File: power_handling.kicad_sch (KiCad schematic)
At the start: 64 parts, among them J1 usb_c, U1 CUS-12TB, U2 TS3USB221ERSER, U3 TPS62130, U4 AP22802AW5-7, U5 MIC5365-1.8YC5-TR, U6 TPS7A0309PDBVR, U7 TPS62130

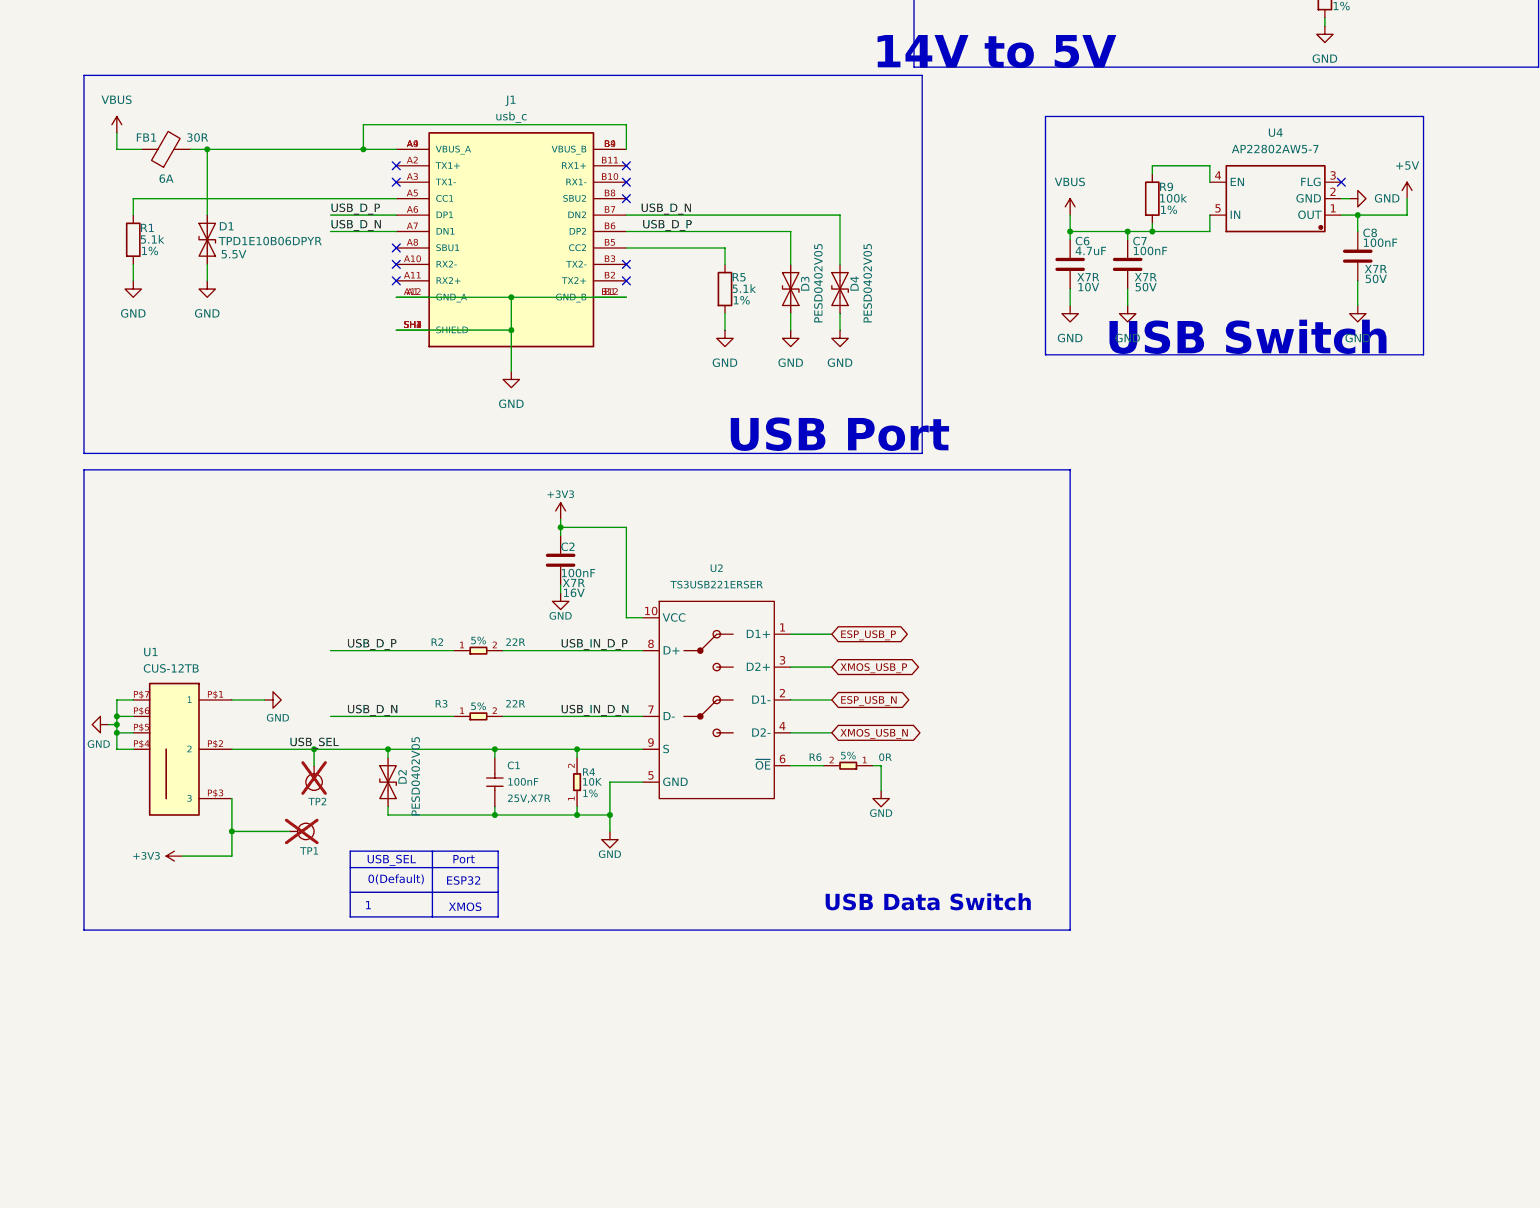
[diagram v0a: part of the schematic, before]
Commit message: adding esp32c6 for OTBR
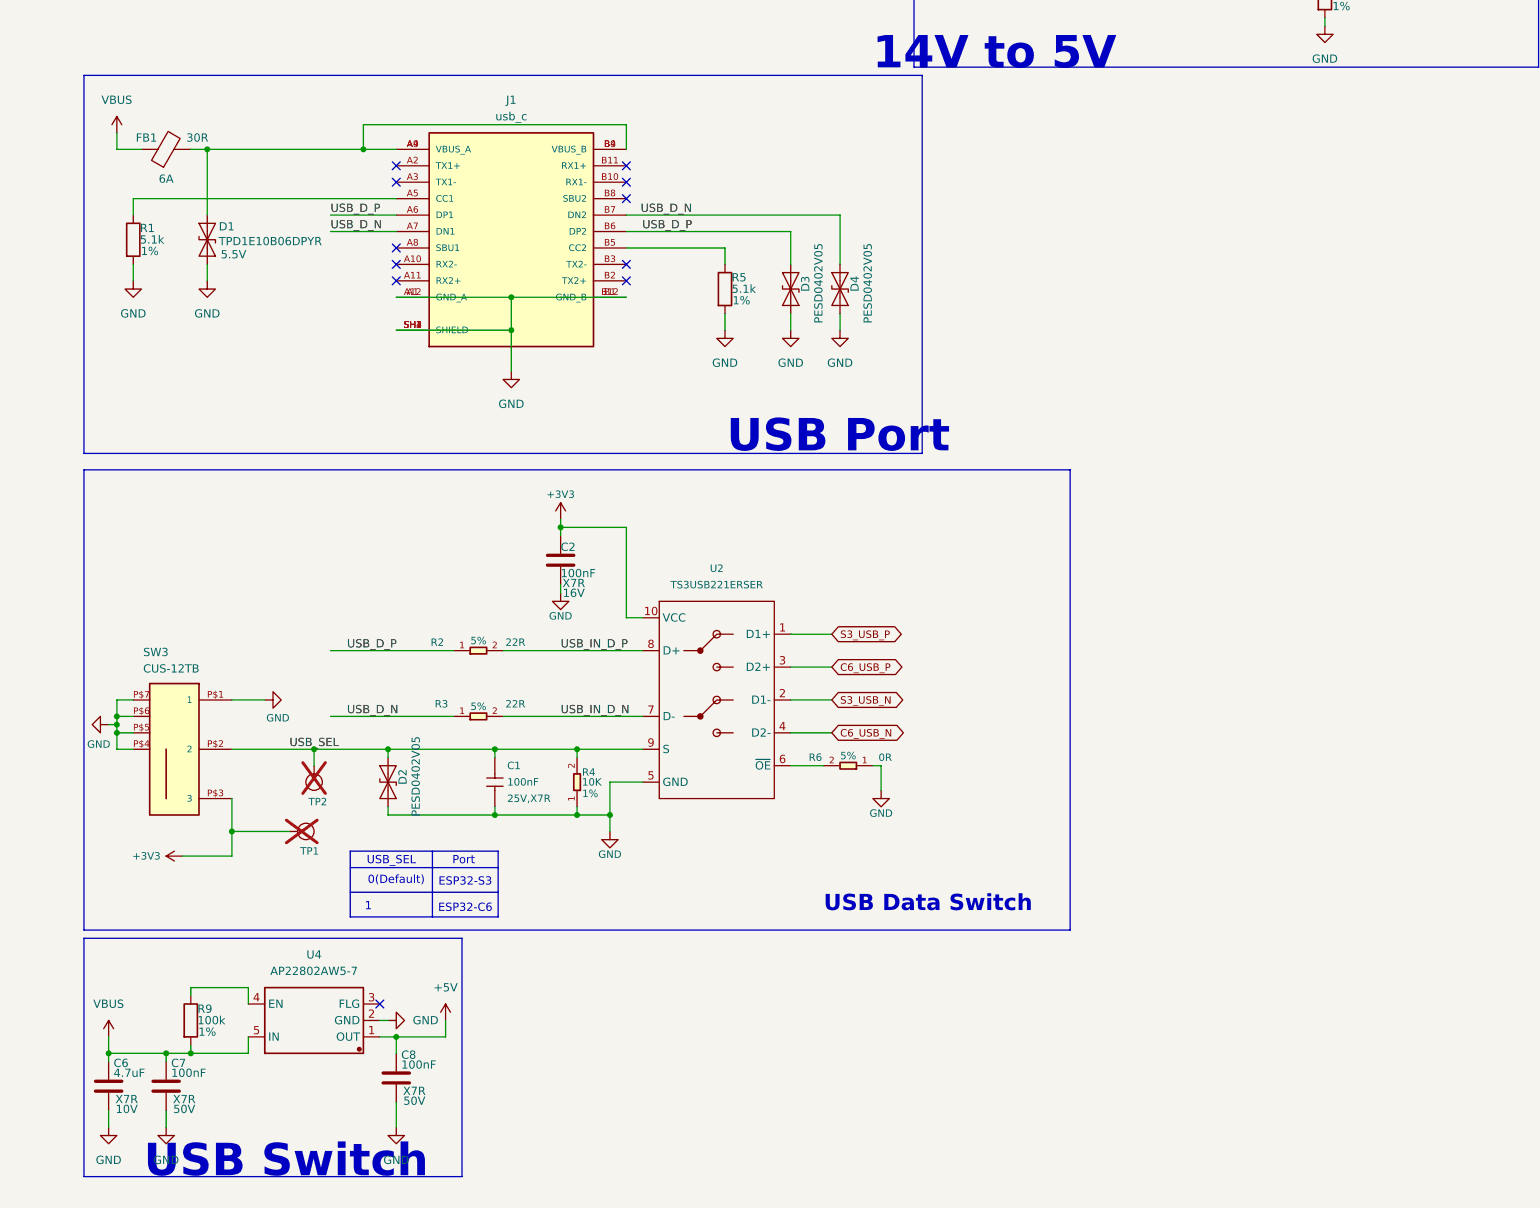
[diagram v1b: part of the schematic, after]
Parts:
- renumbered U1 to SW3
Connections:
- net ESP_USB_N renamed S3_USB_N
- net ESP_USB_P renamed S3_USB_P
- net XMOS_USB_N renamed C6_USB_N
- net XMOS_USB_P renamed C6_USB_P
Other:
- note added: "ESP32-C6"
- note added: "ESP32-S3"
- note removed: "ESP32"
- note removed: "XMOS"
- moved on the sheet: C6, C7, C8, R9, U4

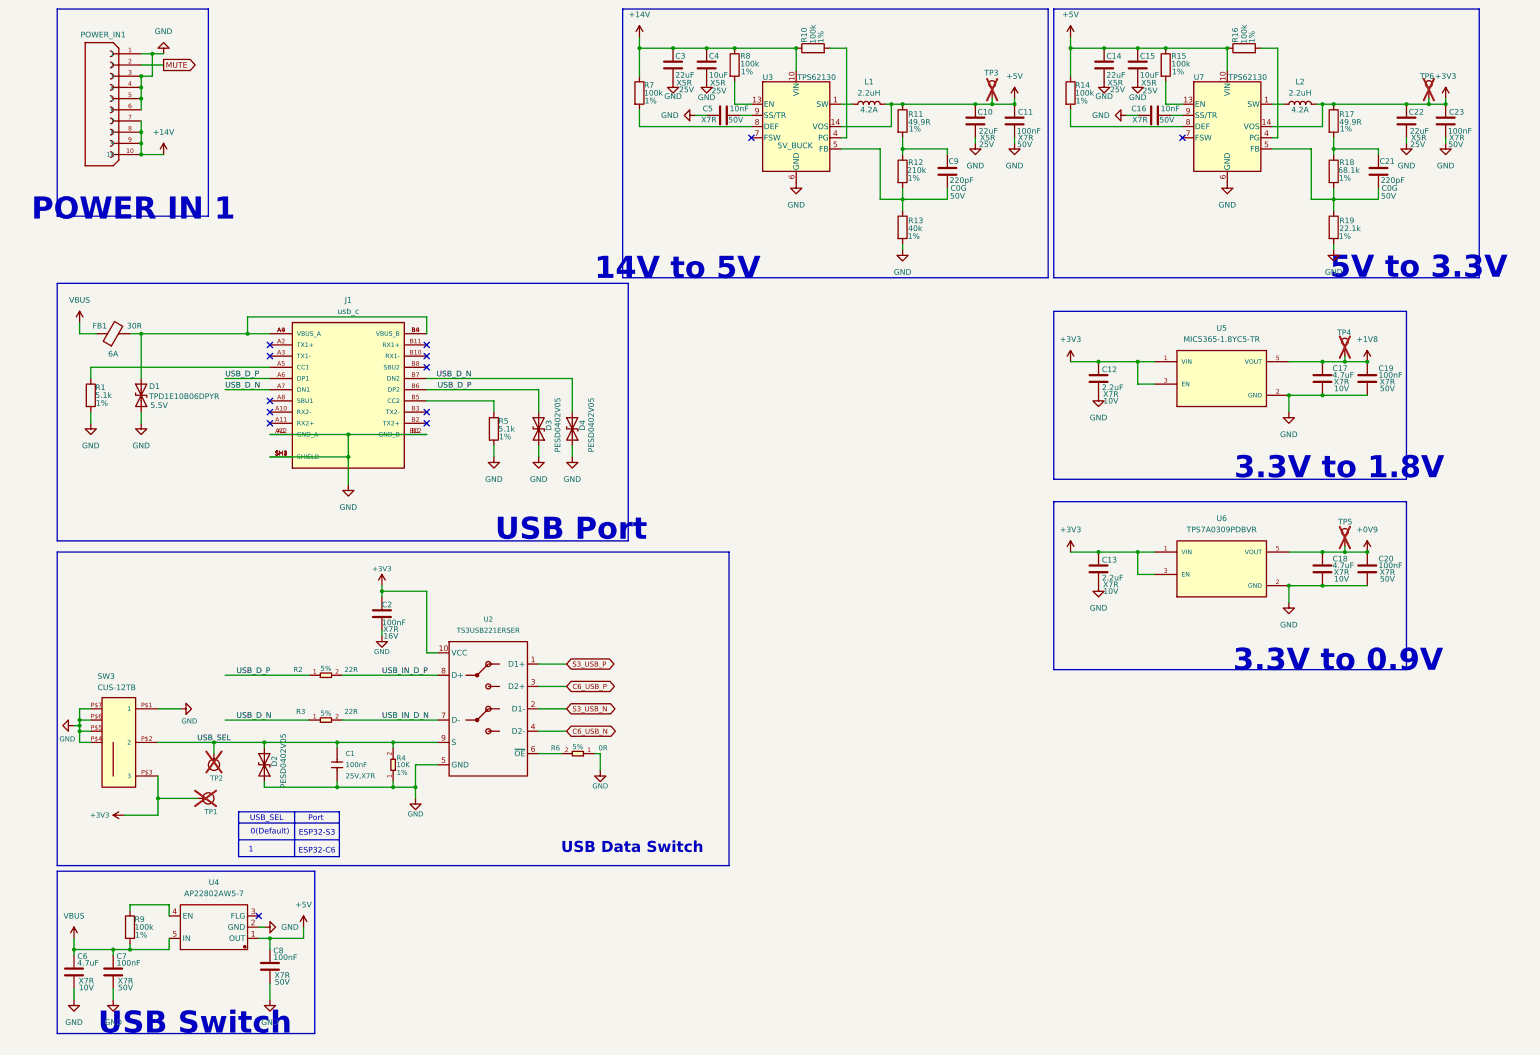
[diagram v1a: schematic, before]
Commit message: Publish KiCad 10 hardware updates
Refresh the Nest Mini v2 drop-in PCB project in KiCad 10 and publish the accumulated schematic and board updates as a single clean mainline change.

Remove the unused USB-C power/input branch from the power sheet, including the USB connector path, data switching, VBUS switching, and associated support parts, while preserving the pogo-accessible USB signals where needed. Add the ESP32-C6 1x05 pogo connector with the J2-style pin order for GND, boot, reset, USB D-, and USB D+ without a 3.3 V pin.

Add a 5 V SN74AHCT1G125 buffer for the LED data input, with local decoupling and a 47 ohm series output resistor, so the LED chain receives a buffered LED_WS2812_5V signal from the ESP_WS2812 control net.

Carry forward the KiCad 10 project save state and schematic cleanups for the XMOS, ESP32, audio, LED, and power sheets without changing the TAS amplifier topology.
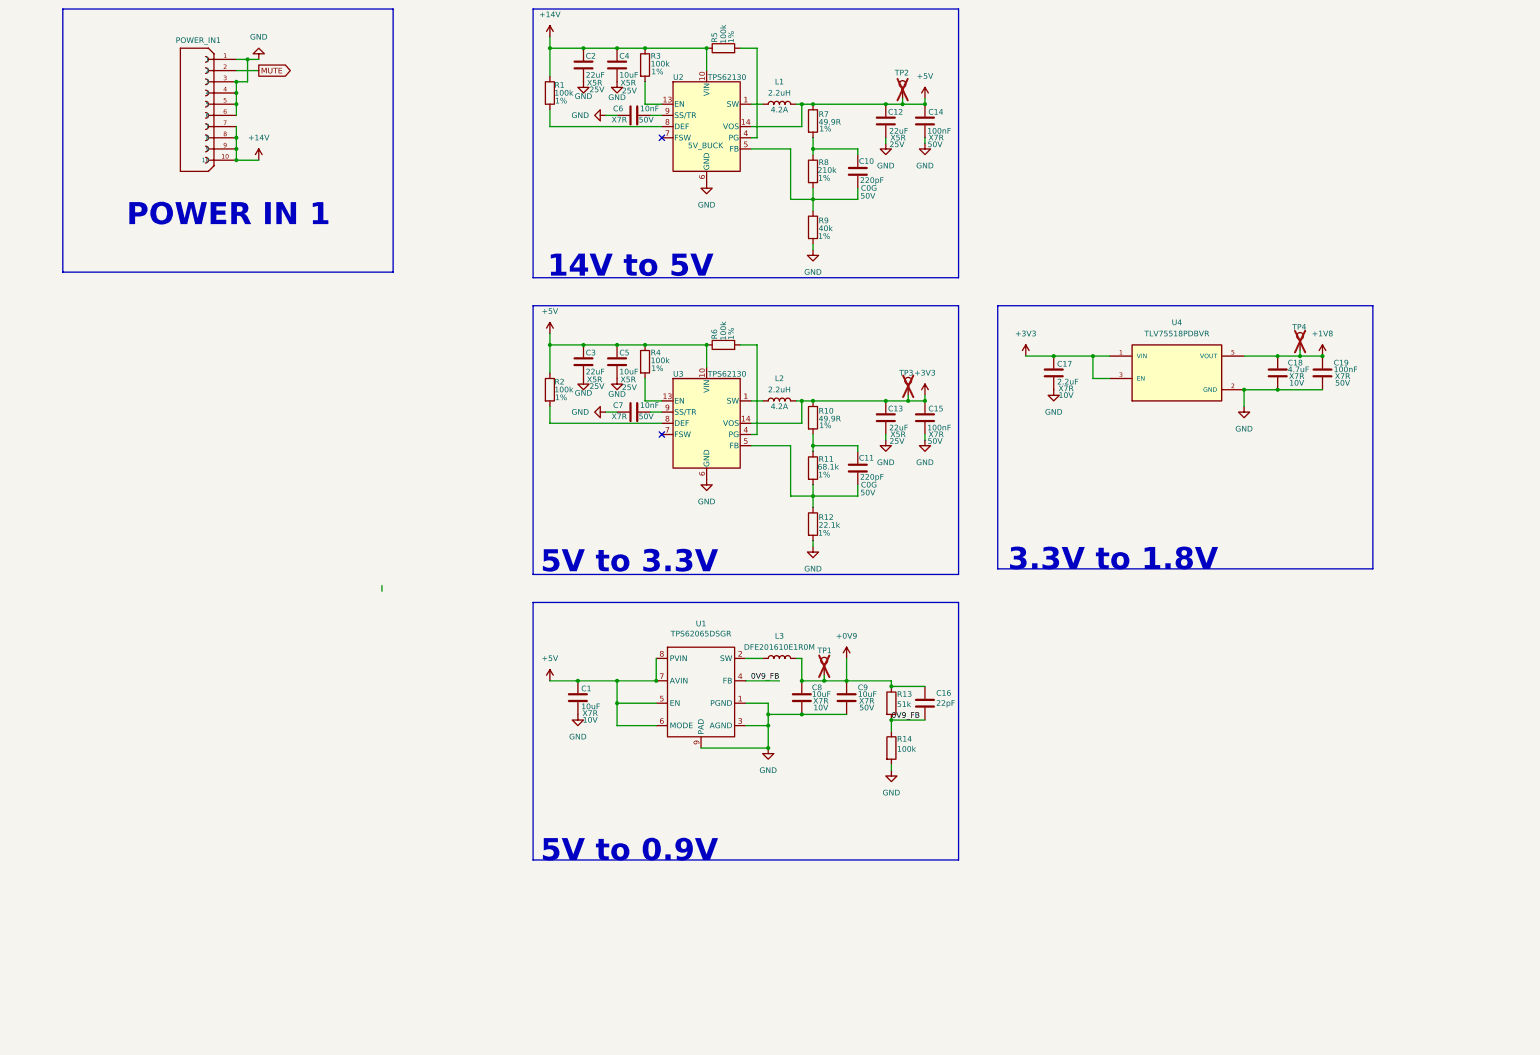
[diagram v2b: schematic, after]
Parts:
- removed C1: 100nF, Capacitor_SMD:C_0402_1005Metric, symbol Seeed_libadl:Capacitors/302010024
- removed C2: 100nF, Capacitor_SMD:C_0402_1005Metric, symbol Device:C
- removed C6: 4.7uF, Capacitor_SMD:C_0603_1608Metric, symbol Device:C
- removed C7, C8: 100nF, Capacitor_SMD:C_0603_1608Metric, symbol Device:C
- removed D1: TPD1E10B06DPYR, Onju:TPD1E05U06DPYR, symbol Diode:SZESD9B5.0ST5G
- removed D2, D3, D4: PESD0402V05, Diode_SMD:D_0402_1005Metric, symbol Diode:SZESD9B5.0ST5G
- removed FB1: 30R, Resistor_SMD:R_0603_1608Metric, symbol Device:FerriteBead
- removed J1: usb_c, Onju:USB-C-SMD_TYPE-C-USB-18, symbol New_Library:usb_c
- removed R1, R5: 5.1k, Resistor_SMD:R_0402_1005Metric, symbol Device:R
- removed R2, R3: 22R, Resistor_SMD:R_0402_1005Metric, symbol Seeed_libadl:Resistors/301010002
- removed R4: 10K, Resistor_SMD:R_0402_1005Metric, symbol Seeed_libadl:Resistors/301010047
- removed R6: 0R, Resistor_SMD:R_0402_1005Metric, symbol Seeed_libadl:Resistors/301010000
- removed R9: 100k, Resistor_SMD:R_0402_1005Metric, symbol Device:R
- removed SW3: CUS-12TB, Onju:CUS-12B, symbol New_Library:CUS-12TB
- removed TP1: Test Point, TestPoint:TestPoint_Pad_D1.0mm, symbol Seeed_libdb:Misc/TP120C_SMD
- removed TP2: Test Point, TestPoint:TestPoint_Pad_D1.0mm, symbol libdb:Misc/TP45C_SMD
- removed U2: TS3USB221ERSER, Onju:TS3USB221ERSER, symbol Seeed_libdb:Ic/310100627
- removed U4: AP22802AW5-7, Package_TO_SOT_SMD:SOT-23-5, symbol New_Library:AP22802AW5-7
- added C16: 22pF, Capacitor_SMD:C_0402_1005Metric, symbol Device:C
- added L3: DFE201610E1R0M, Inductor_SMD:L_Murata_DFE201610P, symbol Device:L
- added R13: 51k, Resistor_SMD:R_0402_1005Metric, symbol Device:R
- added R14: 100k, Resistor_SMD:R_0402_1005Metric, symbol Device:R
- C1: renamed from C13; value 2.2uF -> 10uF; Function 0.9V_LDO -> 0.9V_BUCK_IN
- C8: renamed from C18; value 4.7uF -> 10uF; Function 0.9V_LDO -> 0.9V_BUCK_OUT
- C9: renamed from C20; value 100nF -> 10uF; Function 0.9V_LDO -> 0.9V_BUCK_OUT
- U1: renamed from U6; value TPS7A0309PDBVR -> TPS62065DSGR; footprint Package_TO_SOT_SMD:SOT-23-5 -> Ic:DFN8G-0.5-2X2MM; symbol New_Library:MIC5365-1.8YC5-TR -> New_Library:TPS62065DSGR; Description_1 Linear Voltage Regulator IC Positive Fixed 1 Output 150mA S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 -> 2-A, 3-MHz step-down converter, adjustable output; Function 0.9V_LDO -> 0.9V_BUCK; MF Microchip Technology -> Texas Instruments; MP TPS7A0309PDBVR -> TPS62065DSGR; Manufacturer Part TPS7A0309PDBVR -> TPS62065DSGR; Package SC-70-5 Microchip -> WSON-8 2x2 mm
- U4: renamed from U5; value MIC5365-1.8YC5-TR -> TLV75518PDBVR; footprint Onju:SOT65P210X110-5N -> Package_TO_SOT_SMD:SOT-23-5; Description_1 Linear Voltage Regulator IC Positive Fixed 1 Output 150mA S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 -> Linear voltage regulator, fixed 1.8 V output, 500 mA, SOT-2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; LCSC Part # C626087 -> (none); MANUFACTURER Microchip Tech -> Texas Instruments; MF Microchip Technology -> Texas Instruments; MP MIC5365-1.8YC5-TR -> TLV75518PDBVR; Manufacturer Microchip Tech -> Texas Instruments; Manufacturer Part MIC5365-1.8YC5-TR -> TLV75518PDBVR; Package SC-70-5 Microchip -> SOT-23-5; Supplier Part C626087 -> (none)
- renumbered C9 to C10, C21 to C11, C10 to C12, C22 to C13, C11 to C14, C23 to C15, C12 to C17, C17 to C18, C3 to C2, C14 to C3, C15 to C5, C5 to C6, C16 to C7, R7 to R1, R17 to R10, R18 to R11, R19 to R12, R14 to R2, R8 to R3, R15 to R4, R10 to R5, R16 to R6, R11 to R7, R12 to R8, R13 to R9, TP5 to TP1, TP3 to TP2, TP6 to TP3, U3 to U2, U7 to U3
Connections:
- net +0V9: now also C16.1, L3.2, R13.1; no longer U1.5 (VOUT)
- net +3V3: no longer C1.1, U1.1 (VIN), U1.3 (EN)
- net +5V: now also C1.1, U1.5 (EN), U1.6 (MODE), U1.7 (AVIN), U1.8 (PVIN)
- net GND: now also U1.1 (PGND), U1.3 (AGND), U1.9 (PAD), R14.2; no longer U1.2 (GND)
- new net: L3.1, U1.2 (SW)
- new net 0V9_FB: C16.2, R13.2, R14.1, U1.4 (FB)
- no-connect marks 13 -> 2
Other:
- note added: "5V to 0.9V"
- note removed: "0(Default)"
- note removed: "1"
- note removed: "3.3V to 0.9V"
- note removed: "ESP32-C6"
- note removed: "ESP32-S3"
- note removed: "Port"
- note removed: "USB Data Switch"
- note removed: "USB Port"
- note removed: "USB Switch"
- note removed: "USB_SEL"
- moved on the sheet: C1, C10, C11, C12, C13, C14, C15, C17, C18, C19, C2, C3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
